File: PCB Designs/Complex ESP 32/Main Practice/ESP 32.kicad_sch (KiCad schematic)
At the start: 0 parts

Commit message: Finished Oscillator PCB
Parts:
- added J3: GSD090012SEU, GSD090012SEU:AMPHENOL_GSD090012SEU, symbol GSD090012SEU:GSD090012SEU
- added U2: ESP32-C3-WROOM-02-H4, ESP32-C3-WROOM-02-H4:MODULE_ESP32-C3-WROOM-02-H4, symbol ESP32-C3-WROOM-02-H4:ESP32-C3-WROOM-02-H4
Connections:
- new net: U2.19 (GND), U2.20 (GND), U2.21 (GND), U2.22 (GND), U2.23 (GND), U2.24 (GND), U2.25 (GND), U2.26 (GND), U2.27 (GND), U2.28 (GND), U2.29 (GND), U2.30 (GND), U2.31 (GND), U2.32 (GND), U2.33 (GND), U2.34 (GND), U2.35 (GND), U2.36 (GND), U2.37 (GND), U2.38 (GND), U2.39 (GND), U2.9 (GND)
- new net: J3.G1 (SHIELD_GND), J3.G2 (SHIELD_GND), J3.G3 (SHIELD_GND), J3.G4 (SHIELD_GND)

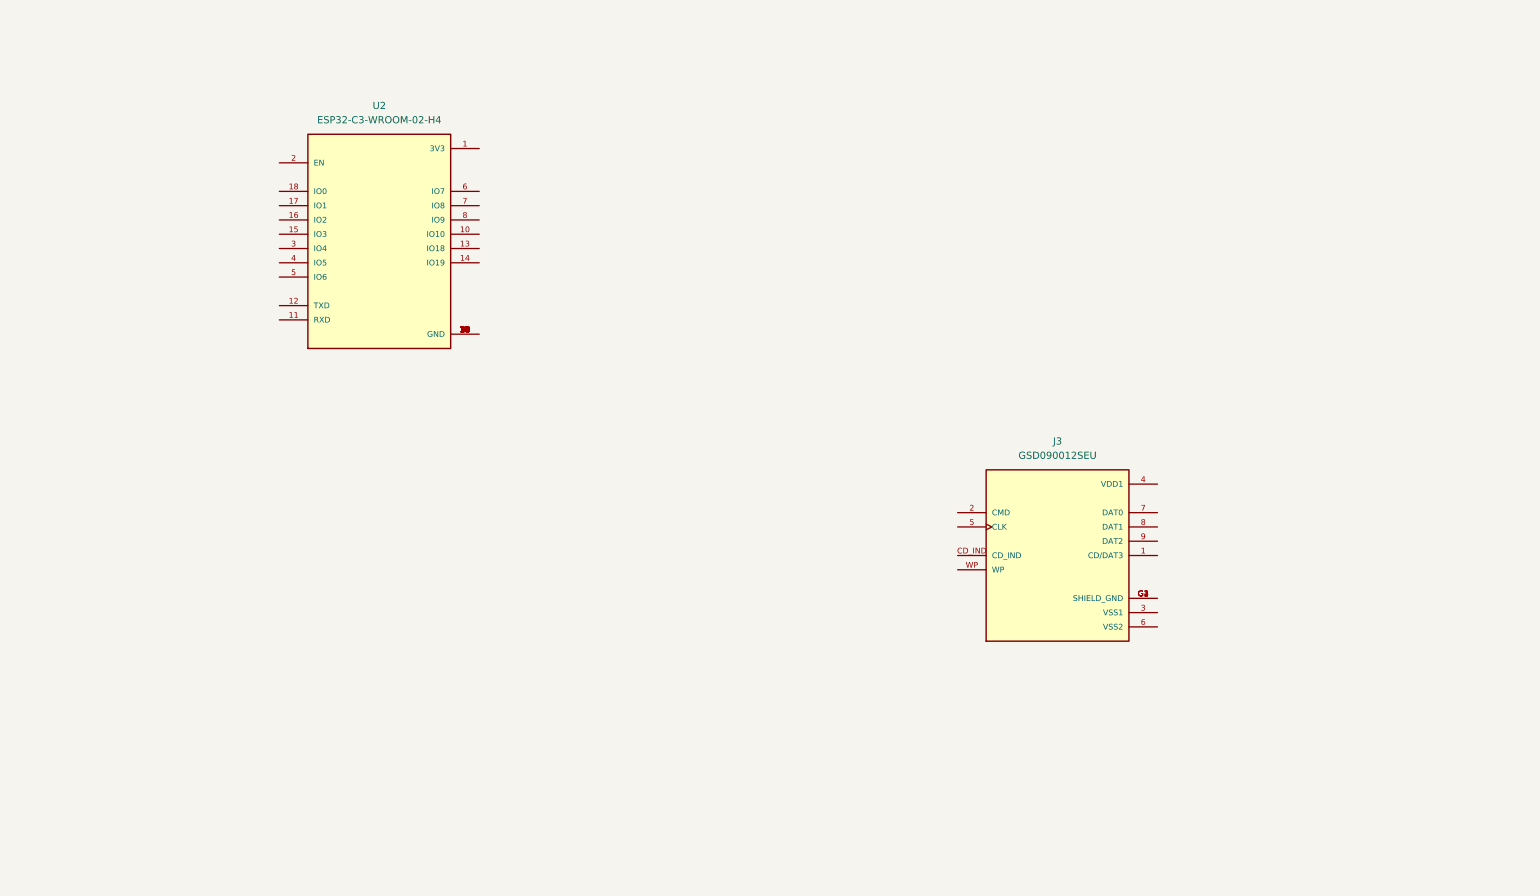
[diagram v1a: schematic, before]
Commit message: Developed upon esp 32 schem
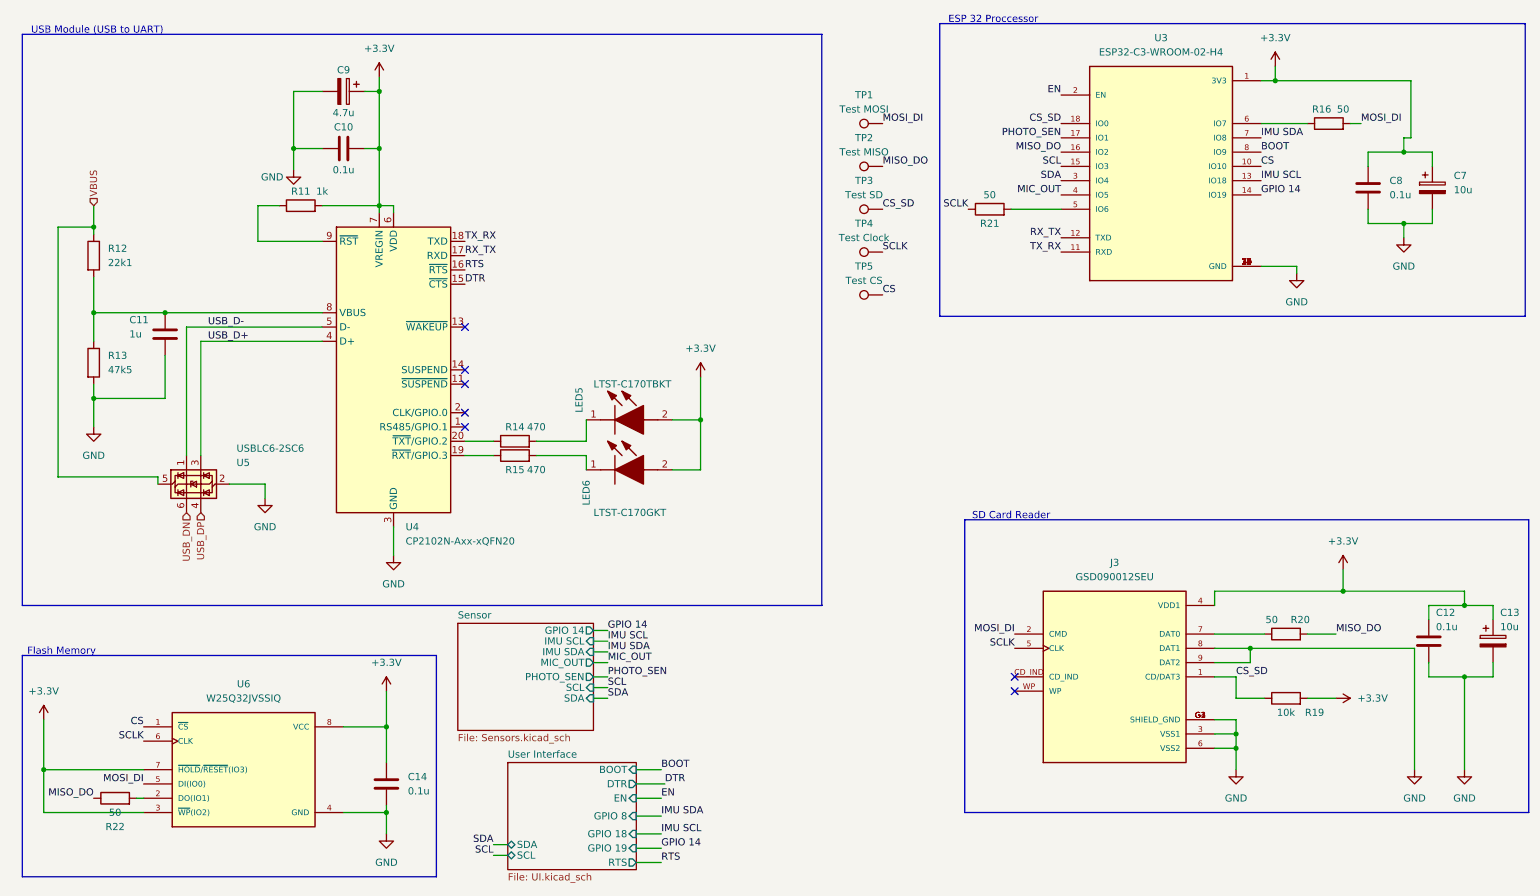
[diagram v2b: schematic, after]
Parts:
- added C10, C12, C14, C8: 0.1u, Capacitor_SMD:C_0805_2012Metric, symbol Device:C
- added C11: 1u, Capacitor_SMD:C_0805_2012Metric, symbol Device:C
- added C13, C7: 10u, Footprints:T491A, symbol Device:C_Polarized
- added C9: 4.7u, Capacitor_SMD:C_0805_2012Metric, symbol Device:C_Polarized
- added LED5: LTST-C170TBKT, Footprints:LEDC2012X120N, symbol LTST-C170TBKT:LTST-C170TBKT
- added LED6: LTST-C170GKT, Footprints:LEDC2012X120N, symbol LTST-C170GKT:LTST-C170GKT
- added R11: 1k, Resistor_SMD:R_0805_2012Metric, symbol Device:R
- added R12: 22k1, Resistor_SMD:R_0805_2012Metric, symbol Device:R
- added R13: 47k5, Resistor_SMD:R_0805_2012Metric, symbol Device:R
- added R14, R15: 470, Resistor_SMD:R_0805_2012Metric, symbol Device:R
- added R16, R20, R21, R22: 50, Resistor_SMD:R_0805_2012Metric, symbol Device:R
- added R19: 10k, Resistor_SMD:R_0805_2012Metric, symbol Device:R
- added TP1: Test MOSI, TestPoint:TestPoint_Pad_D1.0mm, symbol Connector:TestPoint
- added TP2: Test MISO, TestPoint:TestPoint_Pad_D1.0mm, symbol Connector:TestPoint
- added TP3: Test SD, TestPoint:TestPoint_Pad_D1.0mm, symbol Connector:TestPoint
- added TP4: Test Clock, TestPoint:TestPoint_Pad_D1.0mm, symbol Connector:TestPoint
- added TP5: Test CS, TestPoint:TestPoint_Pad_D1.0mm, symbol Connector:TestPoint
- added U4: CP2102N-Axx-xQFN20, Package_DFN_QFN:SiliconLabs_QFN-20-1EP_3x3mm_P0.5mm, symbol Interface_USB:CP2102N-Axx-xQFN20
- added U5: USBLC6-2SC6, Package_TO_SOT_SMD:SOT-23-6, symbol Power_Protection:USBLC6-2SC6
- added U6: W25Q32JVSSIQ, W25Q32JVSSIQ:SOIC127P790X216-8N, symbol Symbols:W25Q32JVSSIQ
- J3: Availability In Stock -> (none); Package None -> (none); Price None -> (none)
- U3: renamed from U2; Availability In Stock -> (none); Package Package -> (none); Price None -> (none); Purchase-URL https://pricing.snapeda.com/search/part/ESP32-C3-WROOM-02-H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 -> (none)
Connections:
- net +3.3V: now reaches U3.1 (3V3)
- net +3.3V: now also J3.4 (VDD1), C10.2, C12.1, C13.1, C14.1, C7.1, C8.1, C9.1, LED5.2 (A), LED6.2 (A), R11.2, R19.2, U4.6 (VDD), U4.7 (VREGIN), U6.3 (~{WP}(IO2)), U6.7 (~{HOLD}/~{RESET}(IO3)), U6.8 (VCC)
- net CS: now reaches U3.10 (IO10)
- net CS: now also TP5.1, U6.1 (~{CS})
- net TX_RX: now reaches U3.11 (RXD)
- net TX_RX: now also U4.18 (TXD)
- net RX_TX: now reaches U3.12 (TXD)
- net RX_TX: now also U4.17 (RXD)
- net IMU SCL: now reaches U3.13 (IO18)
- net GPIO 14: now reaches U3.14 (IO19)
- net SCL: now reaches U3.15 (IO3)
- net MISO_DO: now reaches U3.16 (IO2)
- net MISO_DO: now also R20.2, R22.1, TP2.1
- net PHOTO_SEN: now reaches U3.17 (IO1)
- net CS_SD: now reaches U3.18 (IO0)
- net CS_SD: now also J3.1 (CD/DAT3), R19.1, TP3.1
- net GND: now reaches U3.19 (GND), U3.20 (GND), U3.21 (GND), U3.22 (GND), U3.23 (GND), U3.24 (GND), U3.25 (GND), U3.26 (GND), U3.27 (GND), U3.28 (GND), U3.29 (GND), U3.30 (GND), U3.31 (GND), U3.32 (GND), U3.33 (GND), U3.34 (GND), U3.35 (GND), U3.36 (GND), U3.37 (GND), U3.38 (GND), U3.39 (GND), U3.9 (GND)
- net GND: now also J3.3 (VSS1), J3.6 (VSS2), J3.8 (DAT1), J3.9 (DAT2), J3.G1 (SHIELD_GND), J3.G2 (SHIELD_GND), J3.G3 (SHIELD_GND), J3.G4 (SHIELD_GND), C10.1, C11.2, C12.2, C13.2, C14.2, C7.2, C8.2, C9.2, R13.2, U4.12 (GND), U4.21 (GND), U4.3 (GND), U5.2 (GND), U6.4 (GND)
- net EN: now reaches U3.2 (EN)
- net SDA: now reaches U3.3 (IO4)
- net MIC_OUT: now reaches U3.4 (IO5)
- net at U3.5 (IO6): now also R21.2
- net at U3.6 (IO7): now also R16.1
- net IMU SDA: now reaches U3.7 (IO8)
- net BOOT: now reaches U3.8 (IO9)
- net MOSI_DI: now reaches J3.2 (CMD)
- net MOSI_DI: now also R16.2, TP1.1, U6.5 (DI(IO0))
- net SCLK: now reaches J3.5 (CLK)
- net SCLK: now also R21.1, TP4.1, U6.6 (CLK)
- net at J3.7 (DAT0): now also R20.1
- new net: C11.1, R12.2, R13.1, U4.8 (VBUS)
- new net: R14.1, U4.20 (~{TXT}/GPIO.2)
- new net: LED5.1 (K), R14.2
- new net: R22.2, U6.2 (DO(IO1))
- new net: R11.1, U4.9 (~{RST})
- new net: R15.1, U4.19 (~{RXT}/GPIO.3)
- new net: LED6.1 (K), R15.2
- new net DTR: U4.15 (~{CTS})
- new net RTS: U4.16 (~{RTS})
- new net USB_D+: U4.4 (D+), U5.3 (I/O2)
- new net USB_D-: U4.5 (D-), U5.1 (I/O1)
- new net USB_DN: U5.6 (I/O1)
- new net USB_DP: U5.4 (I/O2)
- new net VBUS: R12.1, U5.5 (VBUS)
- no-connect marks 0 -> 7
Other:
- added sheet Sensor (Sensors.kicad_sch)
- added sheet User Interface (UI.kicad_sch)
- note added: "ESP 32 Proccessor"
- note added: "Flash Memory"
- note added: "SD Card Reader"
- note added: "USB Module (USB to UART)"
- title: (none) -> ESP32 Proccessor
- moved on the sheet: J3, U3

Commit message: Started Schematics of footprint
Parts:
- J3: footprint GSD090012SEU:AMPHENOL_GSD090012SEU -> Footprints:AMPHENOL_GSD090012SEU
- U3: footprint ESP32-C3-WROOM-02-H4:MODULE_ESP32-C3-WROOM-02-H4 -> Footprints:MODULE_ESP32-C3-WROOM-02-H4
- U4: footprint Package_DFN_QFN:SiliconLabs_QFN-20-1EP_3x3mm_P0.5mm -> Package_DFN_QFN:SiliconLabs_QFN-20-1EP_3x3mm_P0.5mm_EP1.8x1.8mm
- U6: footprint W25Q32JVSSIQ:SOIC127P790X216-8N -> Footprints:SOIC127P790X216-8N
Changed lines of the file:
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@@
 			)
 		)
-		(property "Footprint" "Package_DFN_QFN:SiliconLabs_QFN-20-1EP_3x3mm_P0.5mm"
+		(property "Footprint" "Package_DFN_QFN:SiliconLabs_QFN-20-1EP_3x3mm_P0.5mm_EP1.8x1.8mm"
 			(at 113.03 102.87 0)
 			(hide yes)
@@
 			)
 		)
-		(property "Footprint" "W25Q32JVSSIQ:SOIC127P790X216-8N"
+		(property "Footprint" "Footprints:SOIC127P790X216-8N"
 			(at 54.61 147.32 0)
 			(hide yes)
@@
 			)
 		)
-		(property "Footprint" "ESP32-C3-WROOM-02-H4:MODULE_ESP32-C3-WROOM-02-H4"
+		(property "Footprint" "Footprints:MODULE_ESP32-C3-WROOM-02-H4"
 			(at 217.805 42.545 0)
 			(hide yes)
@@
 			)
 		)
-		(property "Footprint" "GSD090012SEU:AMPHENOL_GSD090012SEU"
+		(property "Footprint" "Footprints:AMPHENOL_GSD090012SEU"
 			(at 209.55 130.81 0)
 			(hide yes)

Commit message: reordered components around for optimal wiring
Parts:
- C9: footprint Capacitor_SMD:C_0805_2012Metric -> Footprints:T491A
- renumbered C13 to C12, C12 to C13
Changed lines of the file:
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@@
 			)
 		)
-		(property "Footprint" "Capacitor_SMD:C_0805_2012Metric"
+		(property "Footprint" "Footprints:T491A"
 			(at 68.58 27.6352 0)
 			(hide yes)
@@
 		(in_pos_files yes)
 		(dnp no)
-		(property "Reference" "C12"
+		(property "Reference" "C13"
 			(at 266.7 119.38 0)
 			(show_name no)
@@
 			(project "Main Practice"
 				(path "/3a7f5a9d-c52c-4e05-8447-98c7e4d3dfde/c32656d9-283f-41bc-a7bf-ea6daeb54ad1"
-					(reference "C12")
+					(reference "C13")
 					(unit 1)
 				)
@@
 		(in_pos_files yes)
 		(dnp no)
-		(property "Reference" "C13"
+		(property "Reference" "C12"
 			(at 278.13 119.38 0)
 			(show_name no)
@@
 			(project "Main Practice"
 				(path "/3a7f5a9d-c52c-4e05-8447-98c7e4d3dfde/c32656d9-283f-41bc-a7bf-ea6daeb54ad1"
-					(reference "C13")
+					(reference "C12")
 					(unit 1)
 				)
